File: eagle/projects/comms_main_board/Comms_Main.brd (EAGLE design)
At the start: 101.6 x 95.2 mm, 203 parts, among them J1101 MOL-SL-3-RA, J1102 MOL-SL-2-RA, J1103 MOL-SL-3-RA, J1104 MOL-SL-3-RA, J1105 MOL-SL-3-RA, J1106 MOL-SL-3-RA, J1107 MOL-SL-5-RA, J1108 MOL-SL-2-RA, J1109 MOL-MINIJR-2P-RA, J1110 MOL-MINIJR-2P-RA, J1111 MOL-SL-3-RA, J1112 MOL-SL-2-RA, J1113 MOL-SL-2-RA, J1114 RECEPTACLE-2x2-254MM, J1115 MOL-MINIJR-2P-RA, J1116 MOL-MINIJR-2P-RA, J1117 RECEPTACLE-2x20-254MM, J701 WRL-00593, J801 PRT-12639, J802 PRT-12639, J803 PRT-12639, J804 PRT-12639, Q501 CSD17579Q3A, U1001 MAX3232CSE+, U1002 MAX4311, U401 LP2985-33DBVR, U402 TPS562209DDCT, U403 MAX6371, U501 2N7002P,215, U502 LM3488MMX/NOPB, U503 NDT2955, U601 TPS562209DDCT, U602 TPS562209DDCT, U603 LP5900SD-3.3/NOPB, U701 MAX-M8Q, U801 MMBT3904-HF, U901 PCT2075D,118, U902 MS560702BA03-50, U903 MCP4541-103E/MS

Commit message: Routing
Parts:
- moved TP404 3.41 mm to (37.0, 91.7)
- moved R404 1.17 mm to (40.0, 90.7)
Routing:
- net OSD_DATA: track 2.57 -> 152.1 mm
- net UART_TXD: track 4.92 -> 53.9 mm, vias 0 -> 1
- net WDT_PET: track 8.10 -> 46.3 mm, vias 0 -> 1
- net WDT_BITE_N: track 11.3 -> 46.1 mm, vias 0 -> 1
- net 12V_PI_CONTROLLED: track 13.2 -> 38.6 mm
- net 3P3V_SENSORS: track 101.4 -> 108.3 mm
- added copper zone on layer 1, net WDT_BITE_N

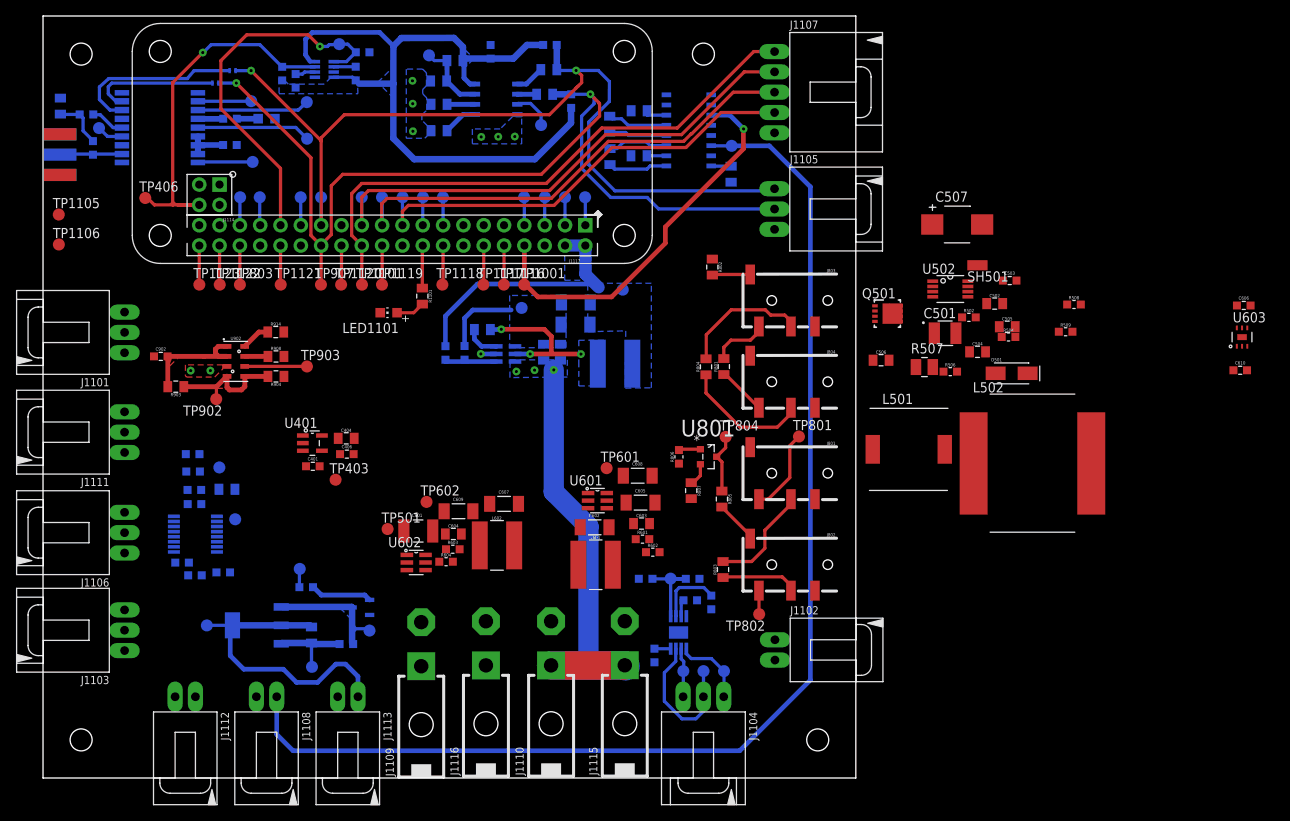
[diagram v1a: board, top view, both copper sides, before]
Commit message: Routed 7.4V to 3.3V power management
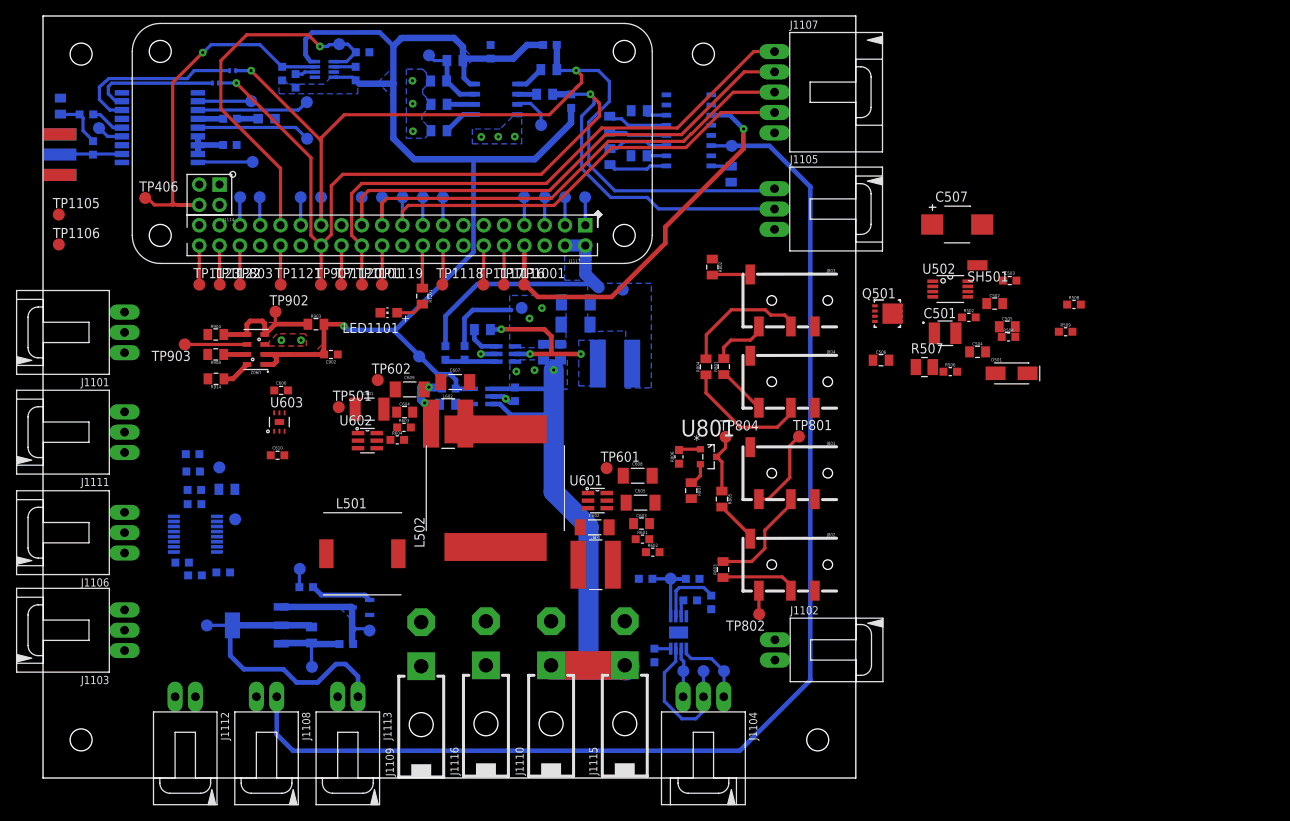
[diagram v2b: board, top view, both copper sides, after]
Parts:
- moved C610 120.8 mm to (29.3, 40.3)
- moved C606 120.8 mm to (29.8, 48.4)
- moved U603 120.8 mm to (29.5, 44.5)
- moved L501 69.5 mm to (39.9, 28.0)
- moved L502 67.2 mm to (56.6, 36.2), turned to 90 degrees
- moved C401 26.8 mm to (59.0, 48.0), flipped to the bottom, turned to 270 degrees
- moved U401 21.9 mm to (54.8, 47.7), flipped to the bottom
- moved C902 21.3 mm to (36.0, 52.9), turned to 180 degrees
- moved R903 19.2 mm to (34.1, 56.7), turned to 0 degrees
- moved TP403 18.6 mm to (47.0, 52.7), flipped to the bottom
- moved C601 16.4 mm to (40.8, 46.1)
- moved C604 16.4 mm to (45.2, 45.7)
- moved R603 16.4 mm to (45.1, 43.8)
- moved TP501 16.4 mm to (37.0, 46.4)
- moved TP602 16.4 mm to (41.8, 49.7)
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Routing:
- net 3P3V_SENSORS: track 108.3 -> 156.8 mm, vias 0 -> 1
- net 7P4V_IN: track 59.2 -> 73.7 mm
- net GND: track 12.5 -> 22.6 mm, vias 8 -> 13
- net SENSOR_LDO_BYPASS: track 0.00 -> 2.06 mm

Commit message: Updated tdocu and tsilk layers of SL connectors used in COMMS board.
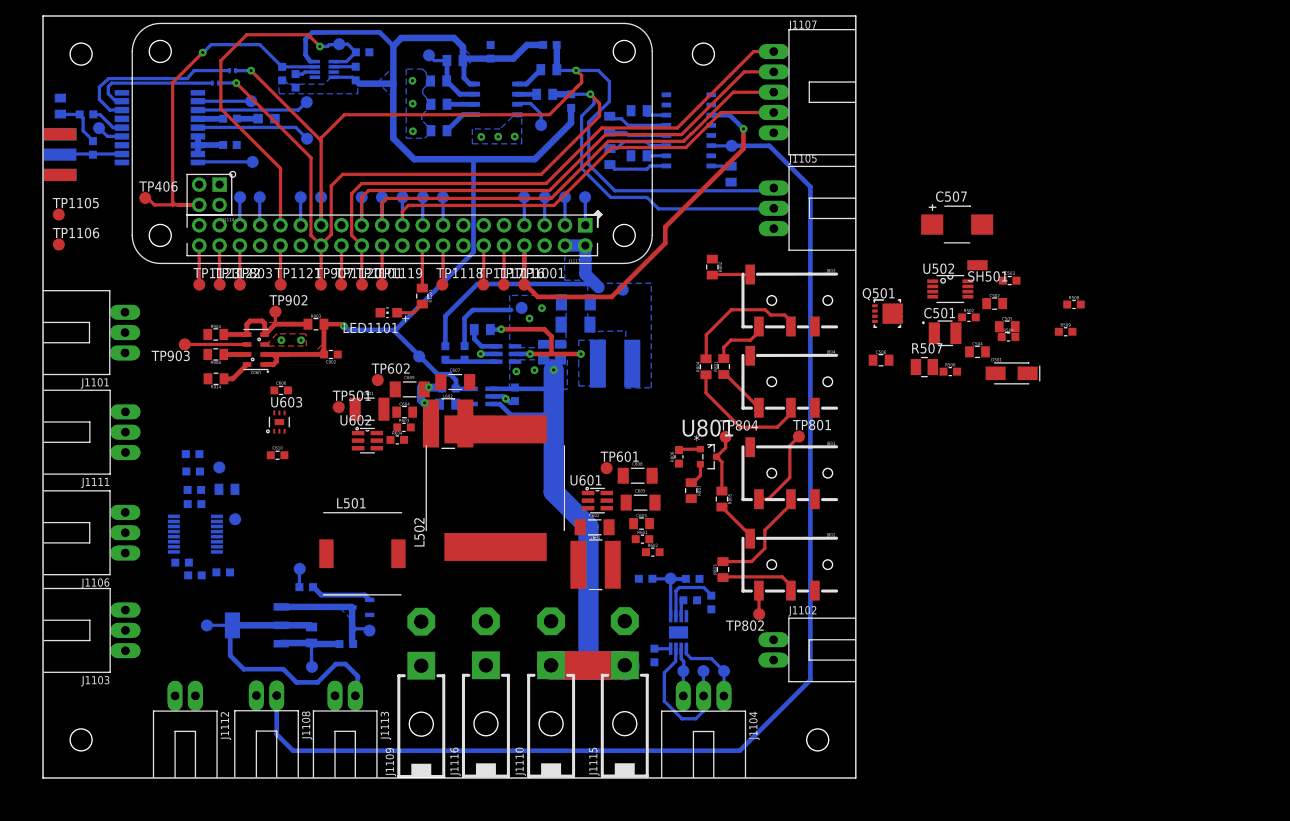
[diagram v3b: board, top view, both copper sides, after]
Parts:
- moved J1113 0.35 mm to (37.8, 2.66)
- moved J1102 0.17 mm to (98.9, 16.0)
- moved J1108 0.15 mm to (27.9, 2.69)
- moved J1105 0.13 mm to (99.0, 71.2)
- moved J1103 0.11 mm to (2.68, 18.5)
- moved J1111 0.11 mm to (2.68, 43.2)
- moved J1112 0.11 mm to (17.8, 2.65)
- moved J1104 0.10 mm to (82.6, 2.64)
- moved J1107 0.10 mm to (99.0, 85.7)
- moved J1106 0.09 mm to (2.66, 30.7)
- moved J1101 0.06 mm to (2.63, 55.7)
- moved J1109 0.06 mm to (47.3, 14.0)

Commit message: Routed 11.1V to 12V
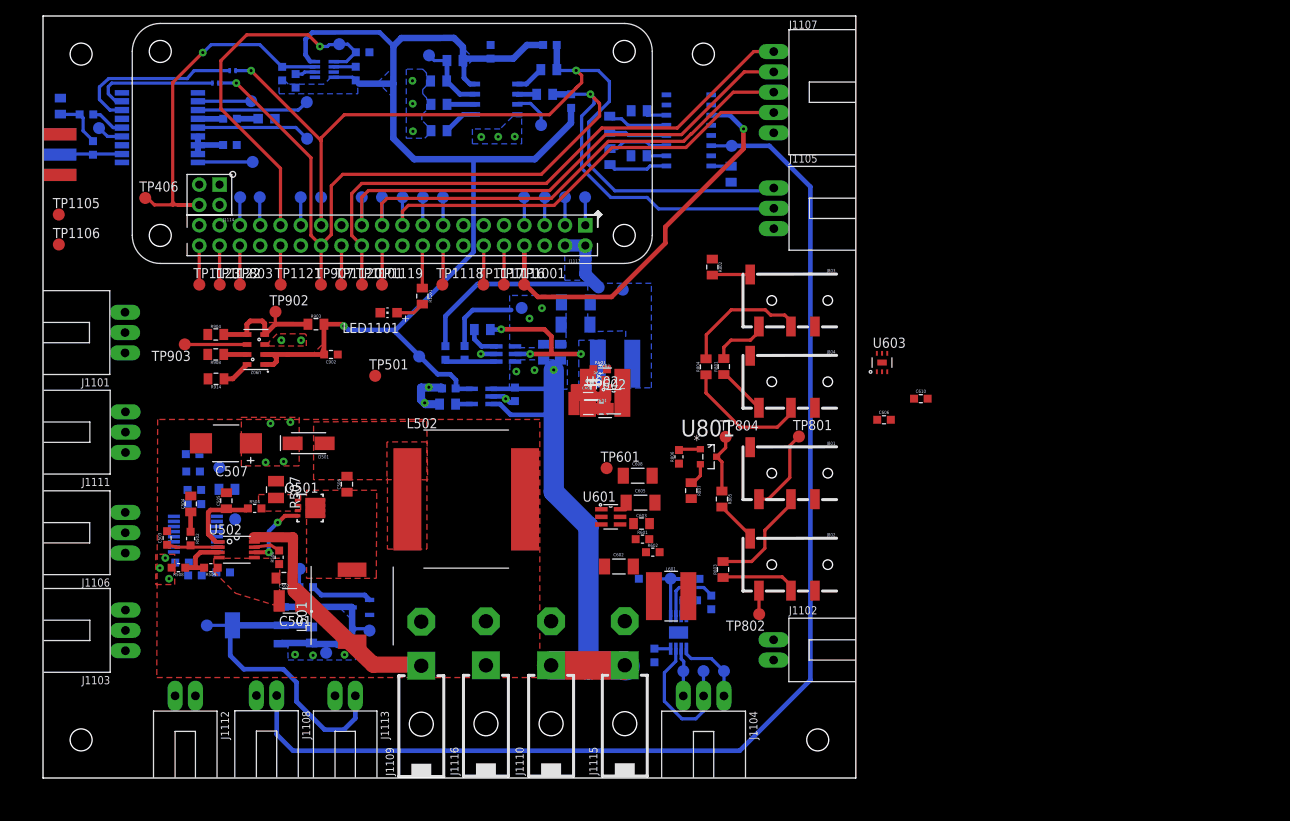
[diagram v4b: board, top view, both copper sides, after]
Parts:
- removed SH501: SHORT-HT5, comms:SHORT_TOP-50
- moved R508 116.7 mm to (16.9, 26.3), turned to 180 degrees
- moved R509 110.8 mm to (21.0, 26.3), turned to 180 degrees
- moved C503 110.1 mm to (15.5, 30.0), turned to 90 degrees
- moved R502 101.1 mm to (18.4, 29.9), turned to 270 degrees
- moved C504 100.2 mm to (18.5, 34.3), turned to 90 degrees
- moved C505 100.0 mm to (22.9, 34.7), turned to 90 degrees
- moved R504 96.6 mm to (26.5, 33.7)
- moved C507 95.4 mm to (22.9, 41.8), turned to 180 degrees
- moved C502 95.2 mm to (30.1, 25.0), turned to 180 degrees
- moved U502 95.0 mm to (24.2, 28.5)
- moved C501 88.5 mm to (30.9, 22.1), turned to 180 degrees
- moved D501 88.3 mm to (33.2, 41.8), turned to 180 degrees
- moved R506 87.0 mm to (29.5, 27.6), turned to 90 degrees
- moved R507 82.5 mm to (29.1, 36.1), turned to 270 degrees
- moved C610 80.7 mm to (109.7, 47.4)
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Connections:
- removed net AGND: SH501.1, U502.4
- net DCDC_STEPUP_ISENSE_RES: now also Q501.2, Q501.3
- net DCDC_STEPUP_OUT: now also Q501.6, Q501.7, Q501.8, Q501.9, Q501.V
- net GND: now also U502.4; no longer SH501.2
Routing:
- net 11P1V_IN: track 0.00 -> 31.4 mm
- net DCDC_STEPUP_ISENSE: track 0.00 -> 9.65 mm
- net DCDC_STEPUP_DR: track 0.00 -> 9.25 mm, vias 0 -> 2
- net DCDC_STEPUP_FB: track 0.00 -> 6.94 mm
- net DCDC_STEPUP_COMP: track 0.00 -> 6.55 mm
- net DCDC_STEPUP_SD: track 0.00 -> 3.31 mm
- net 12V_BOARD: track 10.4 -> 7.38 mm, vias 0 -> 10
- net 12V_PI_CONTROLLED: track 38.5 -> 41.4 mm
- net DCDC_STEPUP_RC_COMP: track 0.00 -> 2.49 mm
- added copper zone on layer 1, net 12V_BOARD
- added copper zone on layer 15, net 12V_BOARD
- added copper zone on layer 16, net 12V_BOARD
- added copper zone on layer 1, net DCDC_STEPUP_ISENSE_RES
- added copper zone on layer 1, net DCDC_STEPUP_OUT
- added copper zone on layer 1, net DCDC_STEPUP_PRE_DIODE

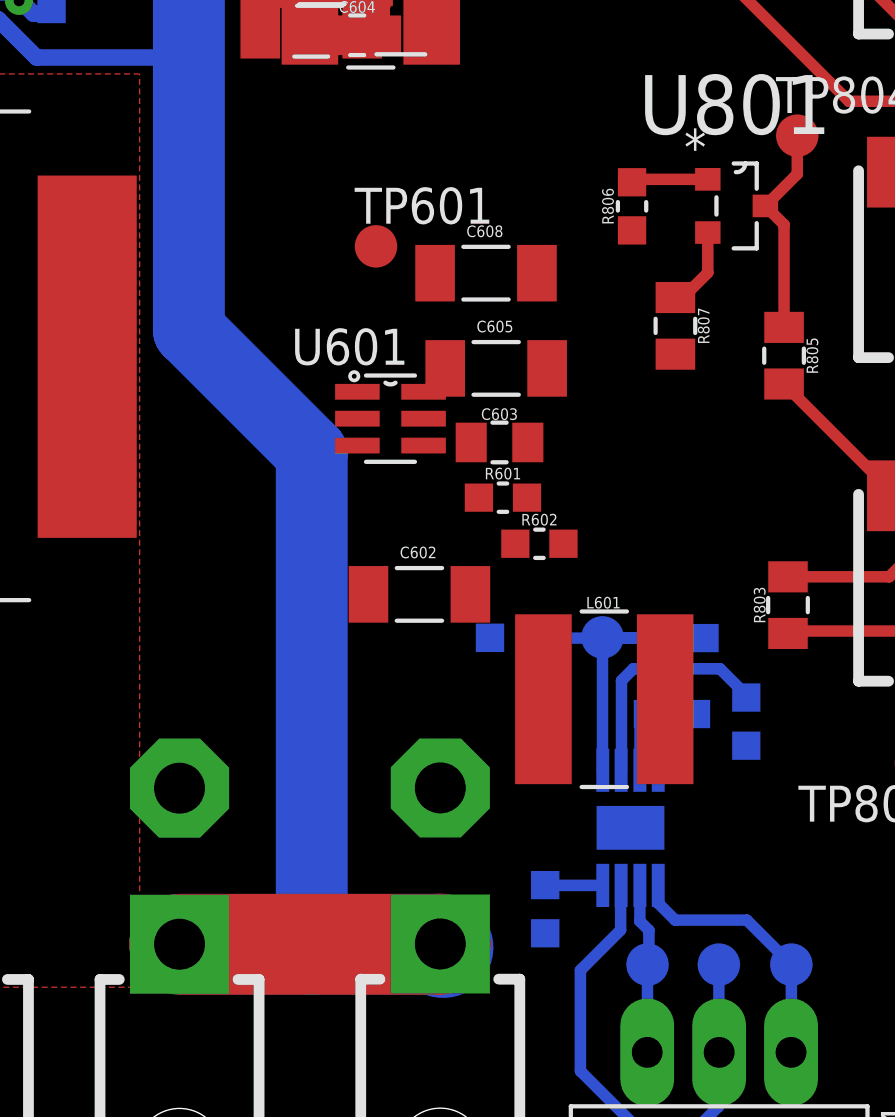
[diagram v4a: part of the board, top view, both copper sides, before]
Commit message: Routed 5V to 3.3V power for digital potentiometer of comms board
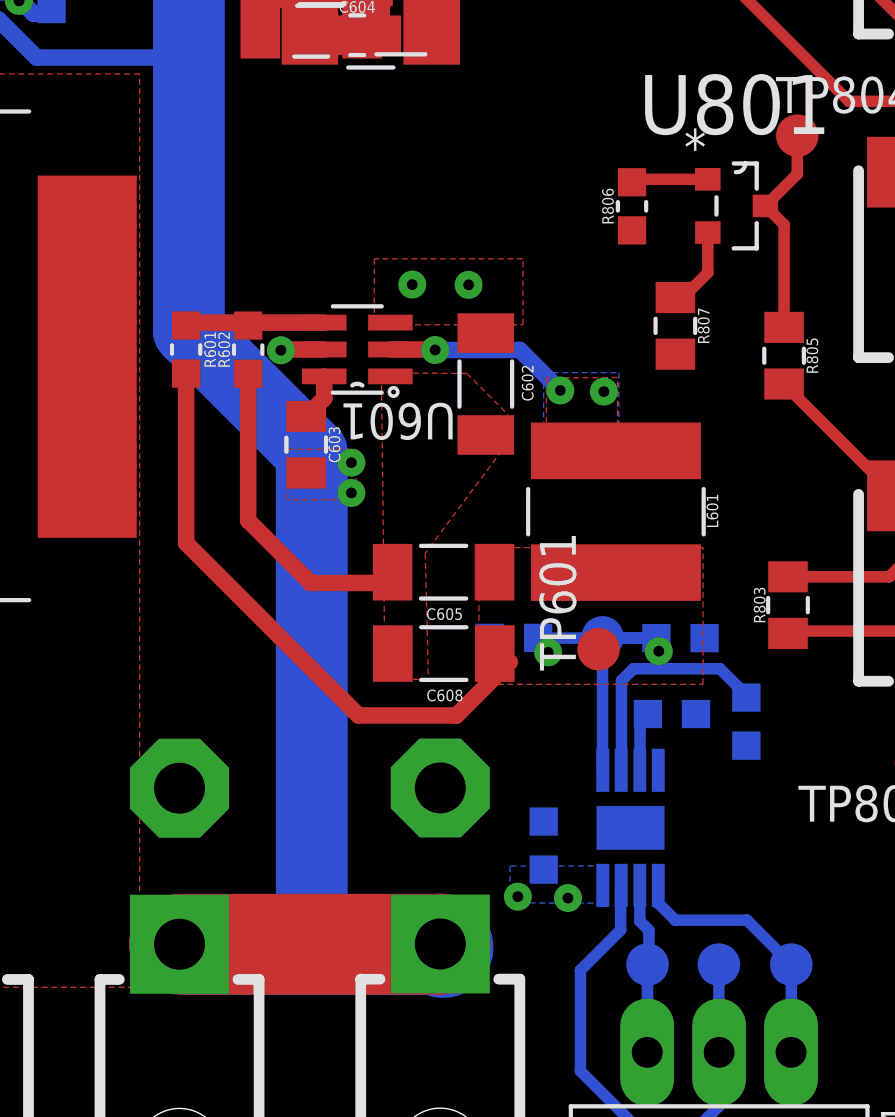
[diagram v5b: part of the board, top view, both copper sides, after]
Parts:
- moved TP601 16.3 mm to (78.3, 24.5), turned to 90 degrees
- moved C608 13.5 mm to (72.8, 24.3), turned to 180 degrees
- moved R602 12.4 mm to (65.9, 35.1), turned to 90 degrees
- moved R601 12.4 mm to (63.7, 35.1), turned to 270 degrees
- moved C602 7.79 mm to (74.3, 33.9), turned to 270 degrees
- moved C605 7.43 mm to (72.8, 27.2), turned to 180 degrees
- moved C603 6.83 mm to (68.0, 31.7), turned to 270 degrees
- moved L601 6.64 mm to (78.9, 29.4), turned to 270 degrees
- moved U601 2.71 mm to (69.8, 35.1), turned to 180 degrees
- moved C903 2.25 mm to (76.4, 17.6), turned to 90 degrees
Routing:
- net 3P3V_DIG_POT: track 2.04 -> 20.7 mm, vias 0 -> 4
- net GND: track 22.6 -> 33.9 mm
- net BUCK_POT_SW: track 0.00 -> 6.61 mm, vias 0 -> 5
- net BUCK_POT_VFB: track 0.00 -> 4.98 mm
- net BUCK_POT_VBST: track 0.00 -> 1.67 mm
- net 5V_BOARD: track 0.00 -> 1.56 mm, vias 0 -> 3
- added copper zone on layer 1, net 3P3V_DIG_POT
- added copper zone on layer 15, net 3P3V_DIG_POT
- added copper zone on layer 16, net 3P3V_DIG_POT
- added copper zone on layer 1, net 5V_BOARD
- added copper zone on layer 15, net 5V_BOARD
- added copper zone on layer 1, net BUCK_POT_SW
- added copper zone on layer 15, net BUCK_POT_SW
- added copper zone on layer 16, net BUCK_POT_SW

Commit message: Finished routing power management for comms board
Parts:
- moved C610 95.8 mm to (17.6, 21.4), turned to 180 degrees
- moved U603 93.3 mm to (17.7, 18.7), turned to 180 degrees
- moved C606 89.1 mm to (20.1, 17.8), turned to 90 degrees
- moved TP602 60.0 mm to (19.5, 13.4)
- moved TP501 36.1 mm to (42.6, 14.2)
- moved TP603 13.1 mm to (20.1, 20.9), flipped to the top
- moved R603 9.78 mm to (60.3, 48.3), turned to 270 degrees
- moved C607 9.32 mm to (68.6, 38.8), turned to 180 degrees
- moved L602 7.73 mm to (74.7, 41.8), turned to 270 degrees
- moved R604 7.09 mm to (62.5, 48.3), turned to 90 degrees
- moved C609 6.66 mm to (68.6, 41.6), turned to 180 degrees
- moved C604 5.58 mm to (64.4, 44.8), turned to 270 degrees
- moved U602 4.99 mm to (66.4, 48.0), turned to 180 degrees
- moved C601 3.69 mm to (71.5, 48.4), turned to 270 degrees
- moved C1002 2.12 mm to (87.9, 76.4), turned to 90 degrees
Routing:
- net 11P1V_IN: track 31.4 -> 59.2 mm, vias 0 -> 6
- net 3P3V_SENSORS: track 156.8 -> 131.1 mm, vias 1 -> 4
- net 5V_BUCK_SW: track 0.00 -> 19.8 mm, vias 0 -> 4
- net 5V_BOARD: track 1.56 -> 21.1 mm, vias 3 -> 5
- net 3P3V_RS232: track 4.80 -> 23.3 mm, vias 0 -> 3
- net 5V_BUCK_VFB: track 0.00 -> 4.99 mm
- net GND: track 33.9 -> 37.7 mm, vias 13 -> 14
- net 7P4V_IN: track 73.7 -> 75.7 mm, vias 4 -> 3
- net 5V_BUCK_VBST: track 0.00 -> 1.59 mm
- added copper zone on layer 1, net 11P1V_IN
- added copper zone on layer 15, net 11P1V_IN
- added copper zone on layer 1, net 3P3V_RS232
- added copper zone on layer 15, net 3P3V_RS232
- added copper zone on layer 15, net 3P3V_SENSORS
- added copper zone on layer 1, net 5V_BUCK_SW
- added copper zone on layer 16, net 5V_BUCK_SW

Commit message: Fixed DRCs, cleaned up board
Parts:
- moved J701 0.25 mm to (2.39, 75.4)
- moved TP705 0.08 mm to (26.0, 84.7)
- moved FB701 0.07 mm to (21.5, 86.8)
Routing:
- net 3P3V_RS232: track 23.3 -> 24.7 mm
